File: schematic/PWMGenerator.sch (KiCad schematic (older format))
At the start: 11 parts, among them J1 Conn_01x02, J2 Conn_01x02, Q1 IRF3205, Q2 IRF3205, SW1 SW_Push, U1 L7805, U2 ATtiny85-20PU

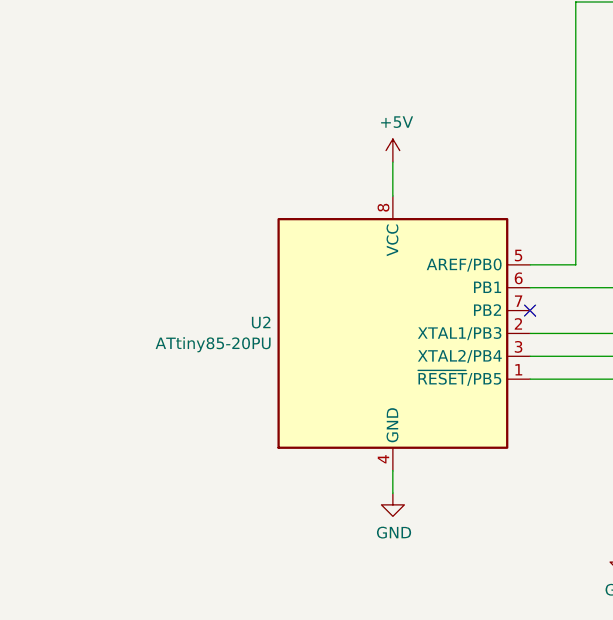
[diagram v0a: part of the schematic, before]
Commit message: schematic: Add missing decoupling capacitor for the attiny
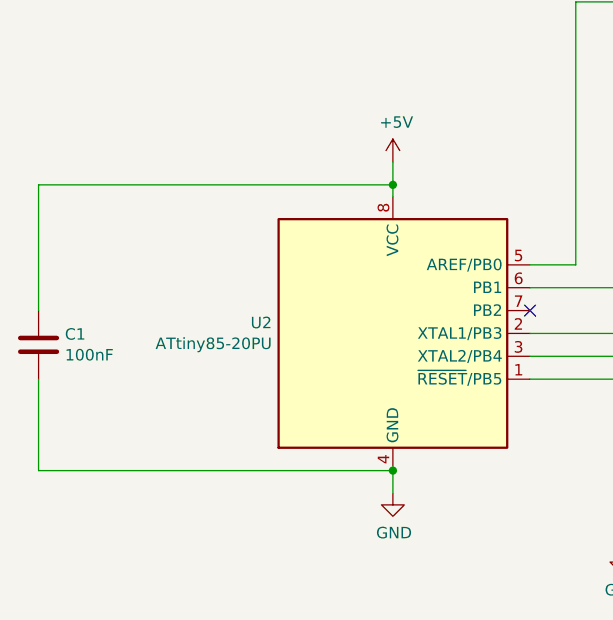
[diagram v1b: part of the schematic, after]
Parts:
- added C1: 100nF, symbol Device:C
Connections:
- net +5V: now also C1.1
- net GND: now also C1.2
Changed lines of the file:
@@
 	5100 5250 5100 5350
 Wire Wire Line
-	5100 3900 5100 4050
+	5100 3900 5100 4000
 Wire Wire Line
 	7750 3400 7750 3500
@@
 Wire Wire Line
 	4100 2550 4100 2700
+$Comp
+L Device:C C1
+U 1 1 5D11FFAE
+P 3550 4700
+F 0 "C1" H 3665 4746 50  0000 L CNN
+F 1 "100nF" H 3665 4655 50  0000 L CNN
+F 2 "" H 3588 4550 50  0001 C CNN
+F 3 "~" H 3550 4700 50  0001 C CNN
+	1    3550 4700
+	1    0    0    -1
+$EndComp
+Wire Wire Line
+	3550 4000 3550 4550
+Connection ~ 5100 4000
+Wire Wire Line
+	5100 4000 5100 4050
+Wire Wire Line
+	3550 4850 3550 5250
+Connection ~ 5100 5250
+Wire Wire Line
+	3550 4000 5100 4000
+Wire Wire Line
+	3550 5250 5100 5250
 $EndSCHEMATC
